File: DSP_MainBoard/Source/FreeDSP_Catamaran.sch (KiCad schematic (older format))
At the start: 251 parts, among them IC1 ADAU1701, IC2 24AA256, IC3 24AA256, J1 Conn_01x02, J10 Conn_01x02, J11 HeaderPin_01x03, J12 B3B-XH, J13 B3B-XH, J14 B3B-XH, J15 Molex 1718563002, J16 Conn_01x03, J2 Conn_RCA, J3 Conn_02x5_Odd_Even, J4 Conn_RCA, J5 Conn_RCA, J6 Conn_RCA, J7 Conn_01x06_Male, J8 Conn_RCA, J9 Conn_Power_2.1mm, P1 MIL-10P_Angle, Q1 2SC3326, Q10 AO3401A, Q11 AO3400A, Q12 AO3401A, Q13 AO3400A, Q2 AO3400A, Q3 2SC3326, Q5 2SC3326, Q6 AO3401A, Q7 2SC3326, Q8 KTA1040D-Y-RTF/P, Q9 AO3400A, SW1 2MS1T1B4M7QES, SW2 2MS1T1B4M7QES, U1 OPA1611, U2 SN74LV541APWR, U3 OPA1611, U4 OPA1611, U5 OPA1611, U6 AZ1117-ADJ, U7 AZ1117-ADJ, U8 OPA1611, U9 OPA1632DR, X2 3N12288G33YC

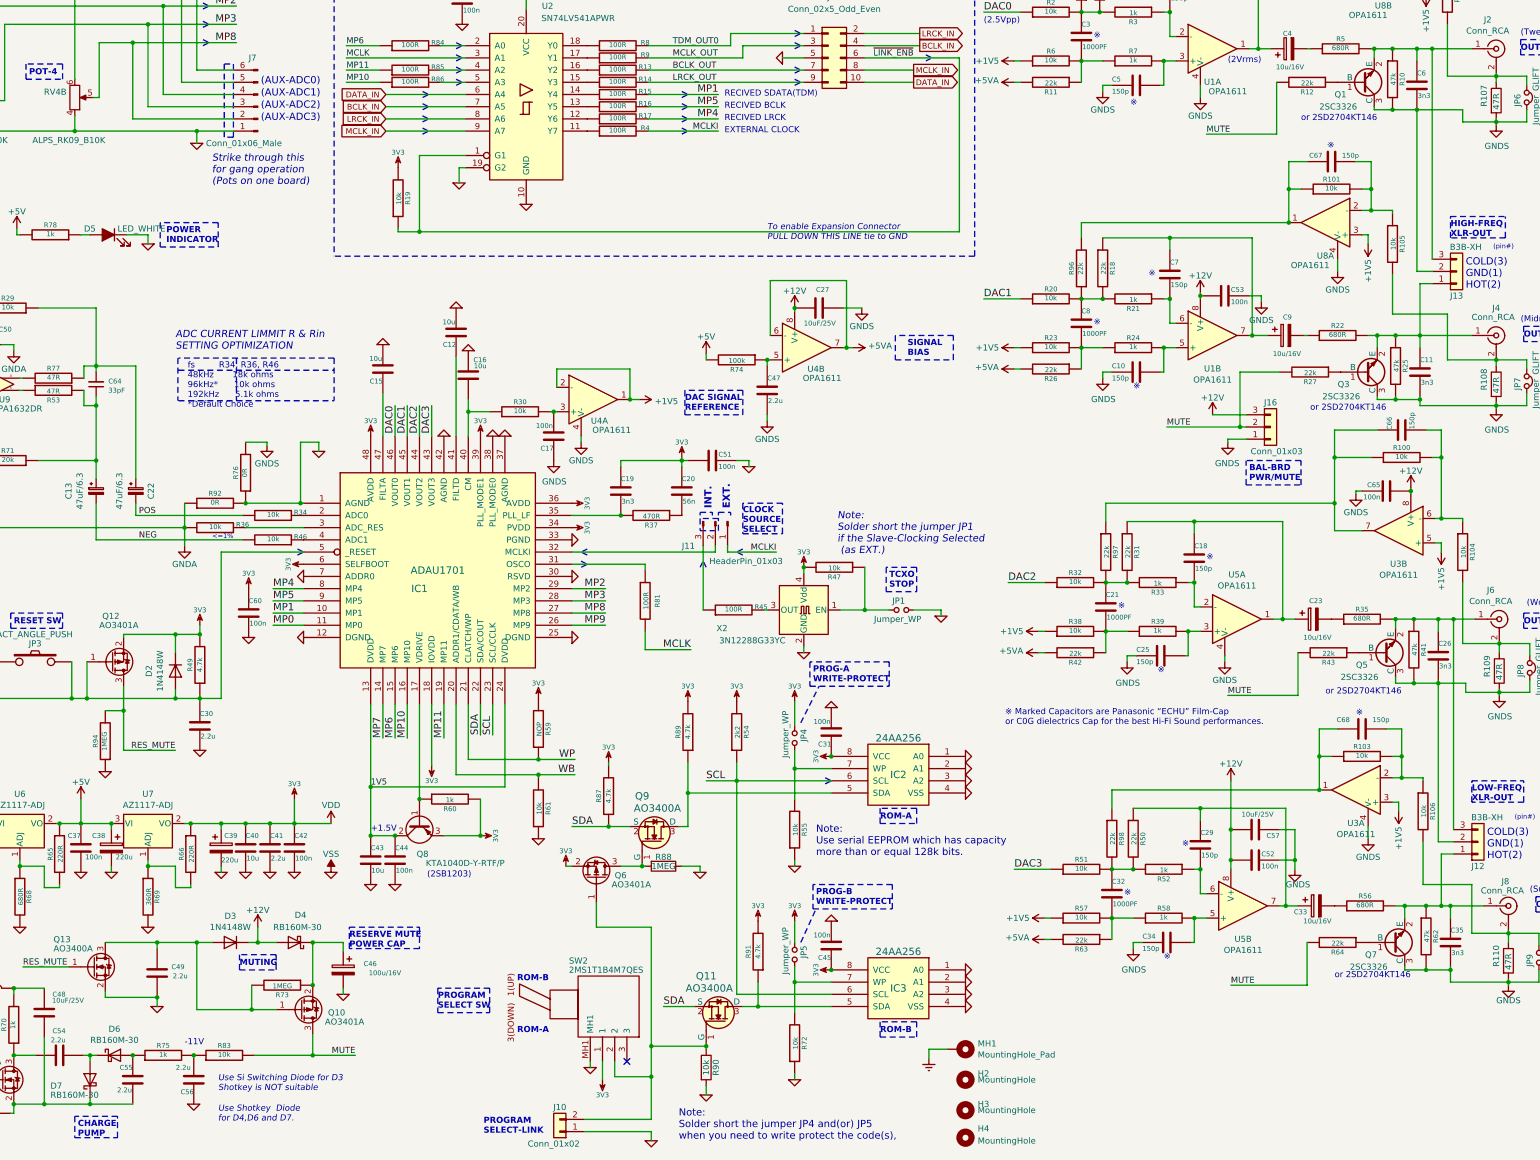
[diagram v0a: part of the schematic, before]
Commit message: FreeDSP Catamaran A/B version 0.21
Changed minor silkscreen layouts
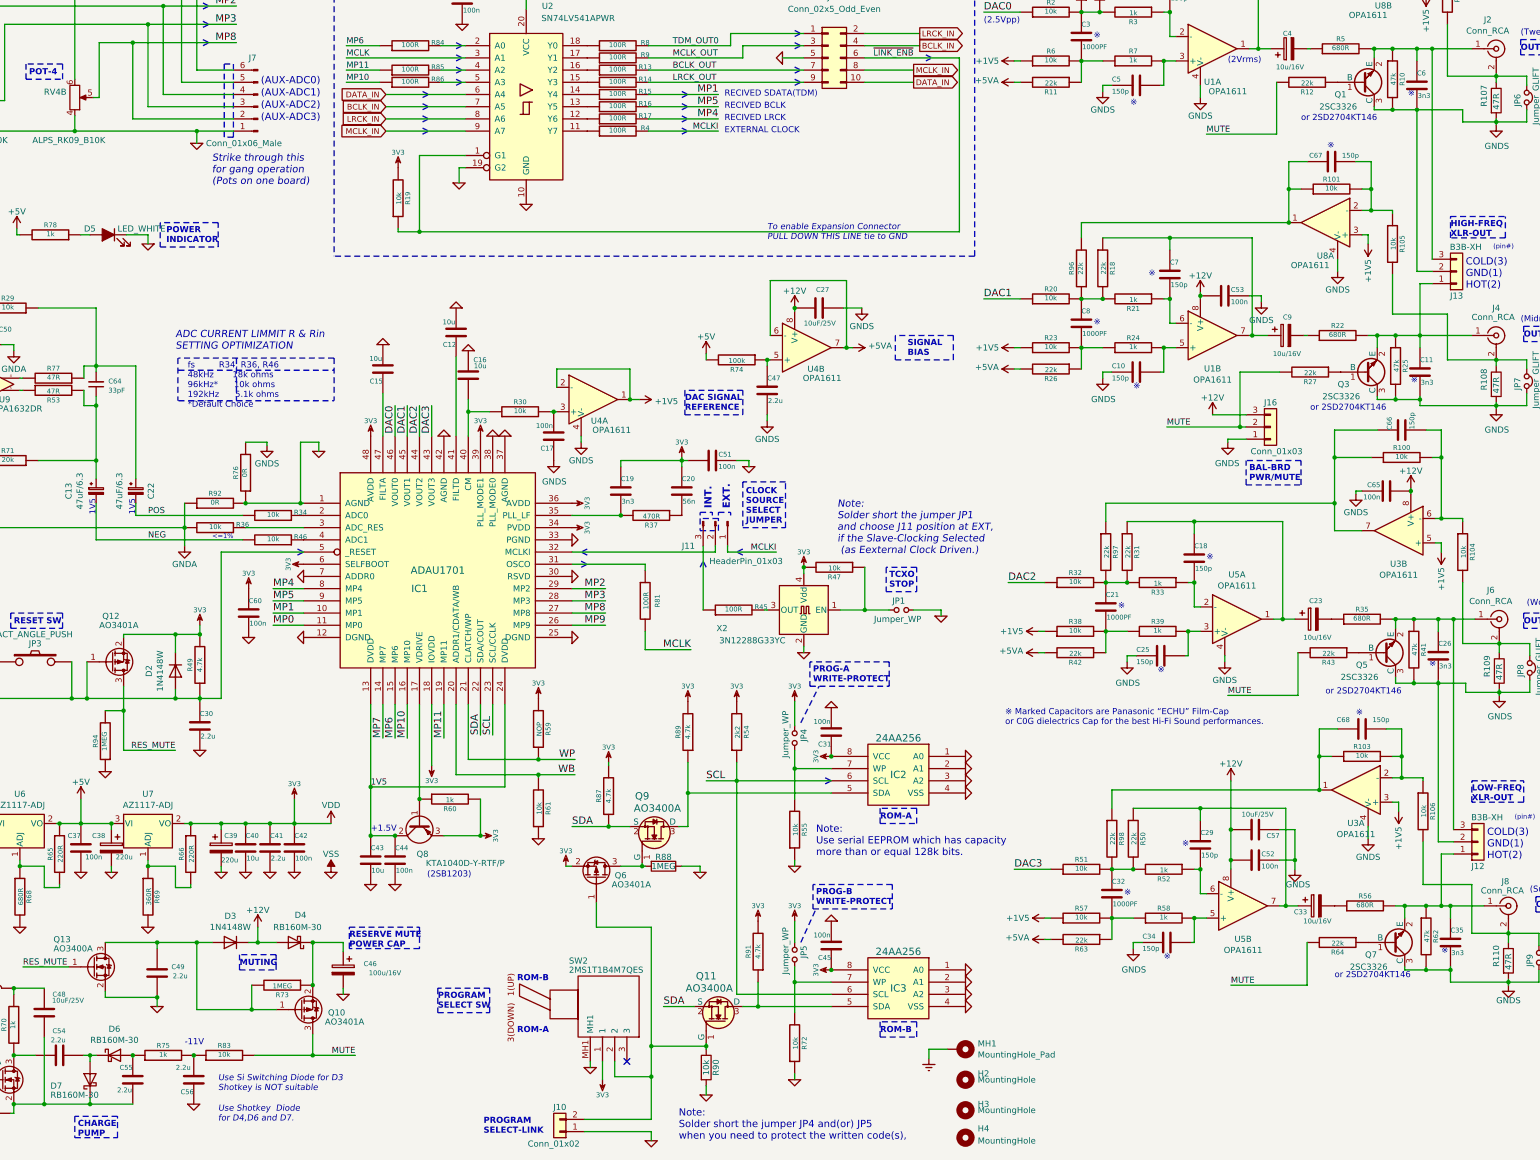
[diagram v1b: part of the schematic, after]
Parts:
- C12, C15, C16, C40, C43, C48, C62: JLPCBA C40894 -> C15850
- D2, D3: JLPCBA C2099 -> C81598
- D4, D6, D7, D8: JLPCBA C130878 -> C8598
- IC1: JLPCBA (none) -> C26394
- Q1, Q3, Q5, Q7: JLPCBA C79973 -> C27829
- R49, R87, R89, R91: JLPCBA C26022 -> C17673
- R73, R88, R94: JLPCBA C26115 -> C17514
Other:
- note added: "1V5"
- note added: "CLOCK\nSOURCE\nSELECT\nJUMPER"
- note added: "Note:\nSolder short the jumper JP1\nand choose J11 position at EXT,\nif the Slave-Clocking Selected\n (as Eexternal Clock Driven.)"
- note added: "Note:\nSolder short the jumper JP4 and(or) JP5 \nwhen you need to protect the written code(s),"
- note removed: "CLOCK\nSOURCE\nSELECT"
- note removed: "Note:\nSolder short the jumper JP1\nif the Slave-Clocking Selected\n (as EXT.)"
- note removed: "Note:\nSolder short the jumper JP4 and(or) JP5 \nwhen you need to write protect the code(s),"
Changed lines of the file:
@@
 F 2 "Housings_QFP:LQFP-48_7x7mm_Pitch0.5mm" H 6525 6500 60  0001 C CNN
 F 3 "" H 6525 6500 60  0000 C CNN
+F 4 "C26394" H 6625 6400 50  0001 C CNN "JLPCBA"
 	1    6625 6400
 	1    0    0    -1
@@
 F 3 "~" H 4675 7175 30  0000 C CNN
 F 4 "SMT" H 4675 7175 50  0001 C CNN "Category"
-F 5 "C26022" H 4675 7175 50  0001 C CNN "JLPCBA"
+F 5 "C17673" H 4675 7175 50  0001 C CNN "JLPCBA"
 	1    4675 7175
 	-1   0    0    1
@@
 F 3 "~" H 6075 8775 60  0000 C CNN
 F 4 "SMT" H 6075 8775 50  0001 C CNN "Category"
-F 5 "C40894" H 6075 8775 50  0001 C CNN "JLPCBA"
+F 5 "C15850" H 6075 8775 50  0001 C CNN "JLPCBA"
 	1    6075 8775
 	1    0    0    -1
@@
 F 3 "~" H 6875 4800 60  0000 C CNN
 F 4 "SMT" H 6875 4800 50  0001 C CNN "Category"
-F 5 "C40894" H 6875 4800 50  0001 C CNN "JLPCBA"
+F 5 "C15850" H 6875 4800 50  0001 C CNN "JLPCBA"
 	1    6875 4800
 	-1   0    0    1
@@
 F 3 "~" H 6775 4450 60  0000 C CNN
 F 4 "SMT" H 6775 4450 50  0001 C CNN "Category"
-F 5 "C40894" H 6775 4450 50  0001 C CNN "JLPCBA"
+F 5 "C15850" H 6775 4450 50  0001 C CNN "JLPCBA"
 	1    6775 4450
 	-1   0    0    1
@@
 F 3 "~" H 6175 4750 60  0000 C CNN
 F 4 "SMT" H 6175 4750 50  0001 C CNN "Category"
-F 5 "C40894" H 6175 4750 50  0001 C CNN "JLPCBA"
+F 5 "C15850" H 6175 4750 50  0001 C CNN "JLPCBA"
 	1    6175 4750
 	-1   0    0    1
@@
 F 3 "~" H 5050 8675 60  0000 C CNN
 F 4 "SMT" H 5050 8675 50  0001 C CNN "Category"
-F 5 "C40894" H 5050 8675 50  0001 C CNN "JLPCBA"
+F 5 "C15850" H 5050 8675 50  0001 C CNN "JLPCBA"
 	1    5050 8675
 	1    0    0    -1
@@
 F 3 "" H 14200 2400 50  0001 L CNN
 F 4 "SMT" H 14200 2400 50  0001 C CNN "Category"
-F 5 "C79973" H 14200 2400 50  0001 C CNN "JLPCBA"
+F 5 "C27829" H 14200 2400 50  0001 C CNN "JLPCBA"
 	1    14200 2400
 	1    0    0    1
@@
 F 3 "" H 14225 4775 50  0001 L CNN
 F 4 "SMT" H 14225 4775 50  0001 C CNN "Category"
-F 5 "C79973" H 14225 4775 50  0001 C CNN "JLPCBA"
+F 5 "C27829" H 14225 4775 50  0001 C CNN "JLPCBA"
 	1    14225 4775
 	1    0    0    1
@@
 F 3 "" H 14375 7075 50  0001 L CNN
 F 4 "SMT" H 14375 7075 50  0001 C CNN "Category"
-F 5 "C79973" H 14375 7075 50  0001 C CNN "JLPCBA"
+F 5 "C27829" H 14375 7075 50  0001 C CNN "JLPCBA"
 	1    14375 7075
 	1    0    0    1
@@
 F 3 "" H 14450 9450 50  0001 L CNN
 F 4 "SMT" H 14450 9450 50  0001 C CNN "Category"
-F 5 "C79973" H 14450 9450 50  0001 C CNN "JLPCBA"
+F 5 "C27829" H 14450 9450 50  0001 C CNN "JLPCBA"
 	1    14450 9450
 	1    0    0    1
@@
 F 3 "~" H 5350 9800 30  0000 C CNN
 F 4 "SMT" H 5350 9800 50  0001 C CNN "Category"
-F 5 "C26115" H 5350 9800 50  0001 C CNN "JLPCBA"
+F 5 "C17514" H 5350 9800 50  0001 C CNN "JLPCBA"
 	1    5350 9800
 	0    1    1    0
@@
 F 3 "~" H 3400 10025 60  0000 C CNN
 F 4 "SMT" H 3400 10025 50  0001 C CNN "Category"
-F 5 "C40894" H 3400 10025 50  0001 C CNN "JLPCBA"
+F 5 "C15850" H 3400 10025 50  0001 C CNN "JLPCBA"
 	1    3400 10025
 	-1   0    0    -1
@@
 F 3 "https://www.vishay.com/docs/85748/1n4148w.pdf" H 4925 9450 50  0001 C CNN
 F 4 "SMT" H 4925 9450 50  0001 C CNN "Category"
-F 5 "C2099" H 4925 9450 50  0001 C CNN "JLPCBA"
+F 5 "C81598" H 4925 9450 50  0001 C CNN "JLPCBA"
 	1    4925 9450
 	-1   0    0    1
@@
 F 3 "~" H 3975 10375 50  0001 C CNN
 F 4 "SMT" H 3975 10375 50  0001 C CNN "Category"
-F 5 "C130878" H 3975 10375 50  0001 C CNN "JLPCBA"
+F 5 "C8598" H 3975 10375 50  0001 C CNN "JLPCBA"
 	1    3975 10375
 	1    0    0    -1
@@
 F 3 "~" H 3775 10575 50  0001 C CNN
 F 4 "SMT" H 3775 10575 50  0001 C CNN "Category"
-F 5 "C130878" H 3775 10575 50  0001 C CNN "JLPCBA"
+F 5 "C8598" H 3775 10575 50  0001 C CNN "JLPCBA"
 	1    3775 10575
 	0    -1   -1   0
@@
 F 3 "~" H 1250 1075 50  0001 C CNN
 F 4 "SMT" H 1250 1075 50  0001 C CNN "Category"
-F 5 "C130878" H 1250 1075 50  0001 C CNN "JLPCBA"
+F 5 "C8598" H 1250 1075 50  0001 C CNN "JLPCBA"
 	1    1250 1075
 	0    -1   -1   0
@@
 F 3 "~" H 5450 9450 50  0001 C CNN
 F 4 "SMT" H 5450 9450 50  0001 C CNN "Category"
-F 5 "C130878" H 5450 9450 50  0001 C CNN "JLPCBA"
+F 5 "C8598" H 5450 9450 50  0001 C CNN "JLPCBA"
 	1    5450 9450
 	-1   0    0    1
@@
 F 3 "https://www.vishay.com/docs/85748/1n4148w.pdf" H 4475 7225 50  0001 C CNN
 F 4 "SMT" H 4475 7225 50  0001 C CNN "Category"
-F 5 "C2099" H 4475 7225 50  0001 C CNN "JLPCBA"
+F 5 "C81598" H 4475 7225 50  0001 C CNN "JLPCBA"
 	1    4475 7225
 	0    1    1    0
 $EndComp
 Text Notes 8600 11075 0    59   ~ 0
-Note:\nSolder short the jumper JP4 and(or) JP5 \nwhen you need to write protect the code(s),
+Note:\nSolder short the jumper JP4 and(or) JP5 \nwhen you need to protect the written code(s),
 Wire Notes Line
 	3650 10875 3650 11050
@@
 F 3 "~" H 3900 7800 30  0000 C CNN
 F 4 "SMT" H 3900 7800 50  0001 C CNN "Category"
-F 5 "C26115" H 3900 7800 50  0001 C CNN "JLPCBA"
+F 5 "C17514" H 3900 7800 50  0001 C CNN "JLPCBA"
 	1    3900 7800
 	-1   0    0    1
@@
 F 3 "" H 8475 8825 30  0000 C CNN
 F 4 "SMT" H 8475 8825 50  0001 C CNN "Category"
-F 5 "C26115" H 8475 8825 50  0001 C CNN "JLPCBA"
+F 5 "C17514" H 8475 8825 50  0001 C CNN "JLPCBA"
 	1    8475 8825
 	0    1    1    0
@@
 F 3 "~" H 8025 8250 30  0000 C CNN
 F 4 "SMT" H 8025 8250 50  0001 C CNN "Category"
-F 5 "C26022" H 8025 8250 50  0001 C CNN "JLPCBA"
+F 5 "C17673" H 8025 8250 50  0001 C CNN "JLPCBA"
 	1    8025 8250
 	-1   0    0    1
@@
 F 3 "~" H 8675 7725 30  0000 C CNN
 F 4 "SMT" H 8675 7725 50  0001 C CNN "Category"
-F 5 "C26022" H 8675 7725 50  0001 C CNN "JLPCBA"
+F 5 "C17673" H 8675 7725 50  0001 C CNN "JLPCBA"
 	1    8675 7725
 	-1   0    0    1
@@
 F 3 "~" H 9250 9525 30  0000 C CNN
 F 4 "SMT" H 9250 9525 50  0001 C CNN "Category"
-F 5 "C26022" H 9250 9525 50  0001 C CNN "JLPCBA"
+F 5 "C17673" H 9250 9525 50  0001 C CNN "JLPCBA"
 	1    9250 9525
 	-1   0    0    1
@@
 Wire Notes Line
 	6475 9325 6475 9500
-Text Label 4175 5950 0    50   ~ 0
+Text Label 4250 5950 0    50   ~ 0
 POS
-Text Label 4175 6150 0    50   ~ 0
+Text Label 4250 6150 0    50   ~ 0
 NEG
 Wire Wire Line
@@
 F 3 "~" H 825 1950 60  0000 C CNN
 F 4 "SMT" H 825 1950 50  0001 C CNN "Category"
-F 5 "C40894" H 825 1950 50  0001 C CNN "JLPCBA"
+F 5 "C15850" H 825 1950 50  0001 C CNN "JLPCBA"
 	1    825  1950
 	-1   0    0    1
@@
 Wire Notes Line
 	8925 5975 8775 5975
-Text Notes 9125 6100 0    50   ~ 10
-CLOCK\nSOURCE\nSELECT
+Text Notes 9150 6025 0    50   ~ 10
+CLOCK\nSOURCE\nSELECT\nJUMPER
 Wire Notes Line
-	9450 6100 9450 5850
+	9475 6050 9475 5675
 Wire Notes Line
-	9450 5850 9125 5850
+	9475 5675 9125 5675
 Wire Notes Line
-	9125 5850 9125 6100
+	9125 5675 9125 6050
 Wire Notes Line
-	9125 6100 9450 6100
+	9125 6050 9475 6050
 Wire Notes Line style solid
 	9125 6275 9075 6250
@@
 Strike through J1\nfor Stereo link
 Text Notes 9900 6275 0    59   Italic 0
-Note:\nSolder short the jumper JP1\nif the Slave-Clocking Selected\n (as EXT.)
+Note:\nSolder short the jumper JP1\nand choose J11 position at EXT,\nif the Slave-Clocking Selected\n (as Eexternal Clock Driven.)
 Text Notes 15050 4100 0    59   ~ 0
 COLD(3)\nGND(1)\nHOT(2)
@@
 	2375 8325 2375 8475
 Connection ~ 2375 8475
+Text Notes 3825 5950 1    49   ~ 0
+1V5
+Text Notes 4150 5950 1    49   ~ 0
+1V5
+Text Notes 14575 2525 0    50   ~ 0
+※
+Text Notes 14600 4875 0    50   ~ 0
+※
+Text Notes 14750 7200 0    50   ~ 0
+※
+Text Notes 14850 9550 0    50   ~ 0
+※
 $EndSCHEMATC

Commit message: Version 1.0 Release Ki-CAD Data Files
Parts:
- added C70: 100n, Capacitors_SMD:C_0805_HandSoldering, symbol Device:C_Small
- J7: value Conn_01x06_Male -> Conn_01x07_Male; footprint Connector_PinHeader_2.54mm:PinHeader_1x06_P2.54mm_Vertical -> Connector_PinHeader_2.54mm:PinHeader_1x07_P2.54mm_Vertical; symbol Connector:Conn_01x06_Male -> Connector:Conn_01x07_Male
- R34, R36, R46: value 10k -> 18k; JLPCBA C17414 -> (none)
- R87, R89, R91: value 4.7k -> 1k; JLPCBA C17673 -> C17513
- U4: value OPA1611 -> OPA1652; JLPCBA C86723 -> C30025
- U4: value OPA1611 -> OPA1652
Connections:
- net +12V: now also U7.3 (VI), C70.1
- net +5V: no longer U7.3 (VI)
- net BRD_~RESET: now also J7.7 (Pin_7)
- net GND: now also C70.2
- net MP0: now also R15.2; no longer R48.1
- net MP1: now also R48.1; no longer R15.2
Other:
- note added: "(96kHz)"
- note added: "(BRD_RESET)"
- note added: "110mA"
- note added: "60mA"
- note added: "AUX-0"
- note added: "AUX-1"
- note added: "AUX-2"
- note added: "AUX-3"
- note added: "MP1 LED\nINDICATOR"
- note added: "fs R34, R36, R46\n48kHz 18k ohms\n96kHz 10k ohms*\n192kHz 5.1k ohms* \n\n*ADC get Noisy Not Recommend\n 18k ohms fits for all."
- note removed: "(48kHz)"
- note removed: "MP0 LED\nINDICATOR"
- note removed: "POT-1"
- note removed: "POT-2"
- note removed: "POT-3"
- note removed: "POT-4"
- note removed: "fs R34, R36, R46\n48kHz 18k ohms\n96kHz* 10k ohms\n192kHz 5.1k ohms\n*Default Choice"
- moved on the sheet: C39, C40, C41, C42, R66, R69, U7
